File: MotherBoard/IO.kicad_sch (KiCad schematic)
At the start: 1 part, among them J1 1376357-3

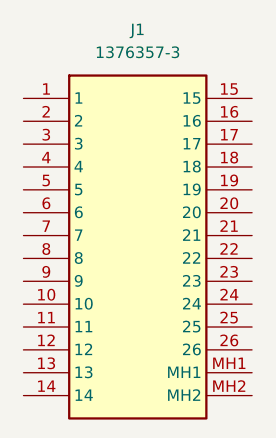
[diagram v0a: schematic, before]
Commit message: Complete bootstrap schematic for MCU
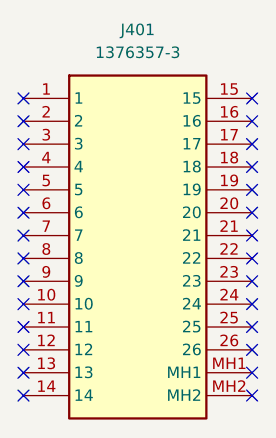
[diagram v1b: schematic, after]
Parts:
- renumbered J1 to J401
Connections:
- no-connect marks 0 -> 28
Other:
- title: IO Connector -> STM32 Layout
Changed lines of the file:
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@@
 	(paper "A4")
 	(title_block
-		(title "IO Connector")
+		(title "STM32 Layout")
 		(date "2024-10-15")
 		(rev "A")
 		(company "FSAE LSU")
+		(comment 1 "Jacob Parent ")
+		(comment 2 "parent.jacob7@protonmail.com")
+	)
+	(no_connect
+		(at 95.25 82.55)
+	)
+	(no_connect
+		(at 95.25 87.63)
+	)
+	(no_connect
+		(at 120.65 100.33)
+	)
+	(no_connect
+		(at 120.65 85.09)
+	)
+	(no_connect
+		(at 95.25 74.93)
+	)
+	(no_connect
+		(at 95.25 95.25)
+	)
+	(no_connect
+		(at 120.65 92.71)
+	)
+	(no_connect
+		(at 95.25 72.39)
+	)
+	(no_connect
+		(at 95.25 102.87)
+	)
+	(no_connect
+		(at 120.65 90.17)
+	)
+	(no_connect
+		(at 95.25 100.33)
+	)
+	(no_connect
+		(at 95.25 85.09)
+	)
+	(no_connect
+		(at 120.65 82.55)
+	)
+	(no_connect
+		(at 95.25 77.47)
+	)
+	(no_connect
+		(at 120.65 105.41)
+	)
+	(no_connect
+		(at 95.25 92.71)
+	)
+	(no_connect
+		(at 120.65 97.79)
+	)
+	(no_connect
+		(at 95.25 80.01)
+	)
+	(no_connect
+		(at 120.65 80.01)
+	)
+	(no_connect
+		(at 95.25 105.41)
+	)
+	(no_connect
+		(at 120.65 74.93)
+	)
+	(no_connect
+		(at 95.25 97.79)
+	)
+	(no_connect
+		(at 120.65 72.39)
+	)
+	(no_connect
+		(at 120.65 77.47)
+	)
+	(no_connect
+		(at 95.25 90.17)
+	)
+	(no_connect
+		(at 120.65 102.87)
+	)
+	(no_connect
+		(at 120.65 87.63)
+	)
+	(no_connect
+		(at 120.65 95.25)
 	)
 	(symbol
@@
 		(dnp no)
 		(fields_autoplaced yes)
-		(property "Reference" "J1"
+		(property "Reference" "J401"
 			(at 107.95 64.77 0)
 			(effects
@@
 		(pin "23"
 		)
-		(instances
-			(project ""
-				(path "/335e81e9-b957-4266-8116-dde74329bfca/a79abe16-9d7e-418f-82e9-de5f72e3bb16"
-					(reference "J1")
-					(unit 1)
-				)
-			)
-		)
+		(instances)
 	)
 )

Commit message: PSU Complete
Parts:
- renumbered J401 to J301
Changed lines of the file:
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@@
 		(dnp no)
 		(fields_autoplaced yes)
-		(property "Reference" "J401"
+		(property "Reference" "J301"
 			(at 107.95 64.77 0)
 			(effects
@@
 		(pin "23"
 		)
-		(instances)
+		(instances
+			(project ""
+				(path "/335e81e9-b957-4266-8116-dde74329bfca/a79abe16-9d7e-418f-82e9-de5f72e3bb16"
+					(reference "J301")
+					(unit 1)
+				)
+			)
+		)
 	)
 )

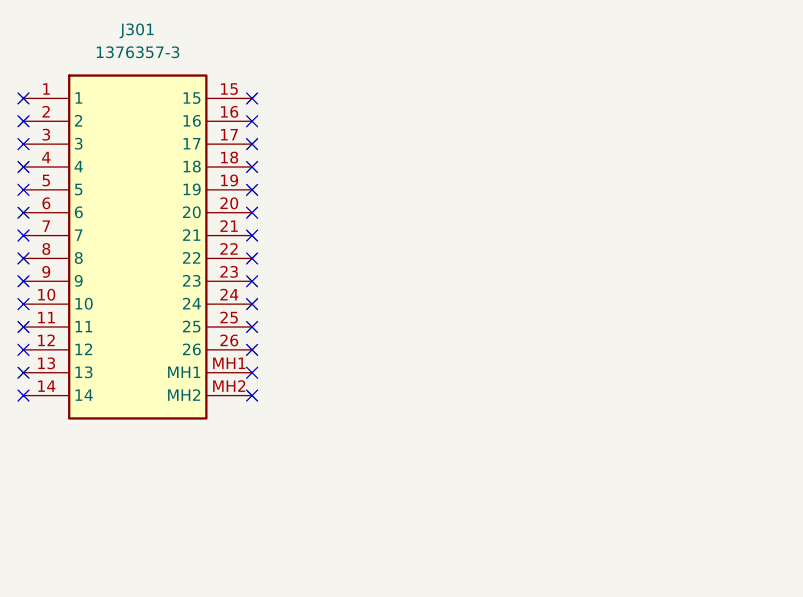
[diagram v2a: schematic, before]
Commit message: Added BQ7900 rough draft and TCAN
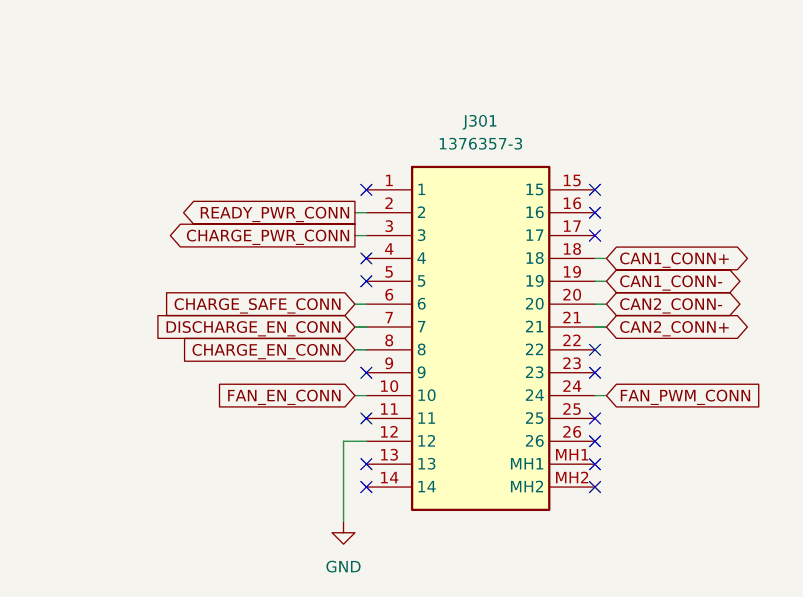
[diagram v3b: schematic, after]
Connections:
- net FAN_EN_CONN: now reaches J301.10
- net GND: now reaches J301.12
- net CAN1_CONN+: now reaches J301.18
- net CAN1_CONN-: now reaches J301.19
- net READY_PWR_CONN: now reaches J301.2
- net CAN2_CONN-: now reaches J301.20
- net CAN2_CONN+: now reaches J301.21
- net FAN_PWM_CONN: now reaches J301.24
- net CHARGE_PWR_CONN: now reaches J301.3
- net CHARGE_SAFE_CONN: now reaches J301.6
- net DISCHARGE_EN_CONN: now reaches J301.7
- net CHARGE_EN_CONN: now reaches J301.8
- no-connect marks 28 -> 16
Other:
- moved on the sheet: J301

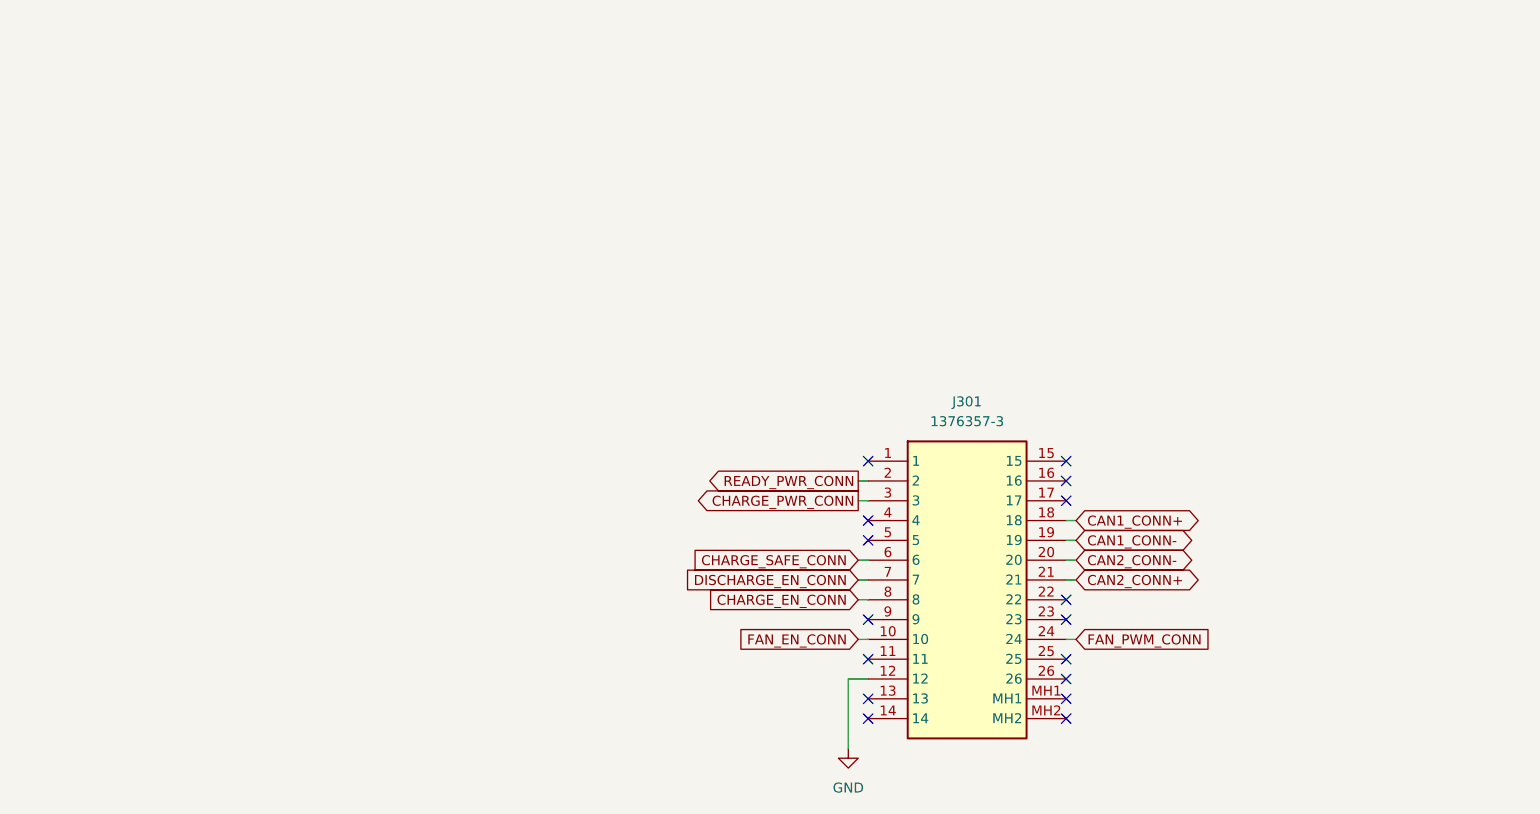
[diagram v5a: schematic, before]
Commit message: Fixed 3D model paths. Finished PSU ORing shcematic.
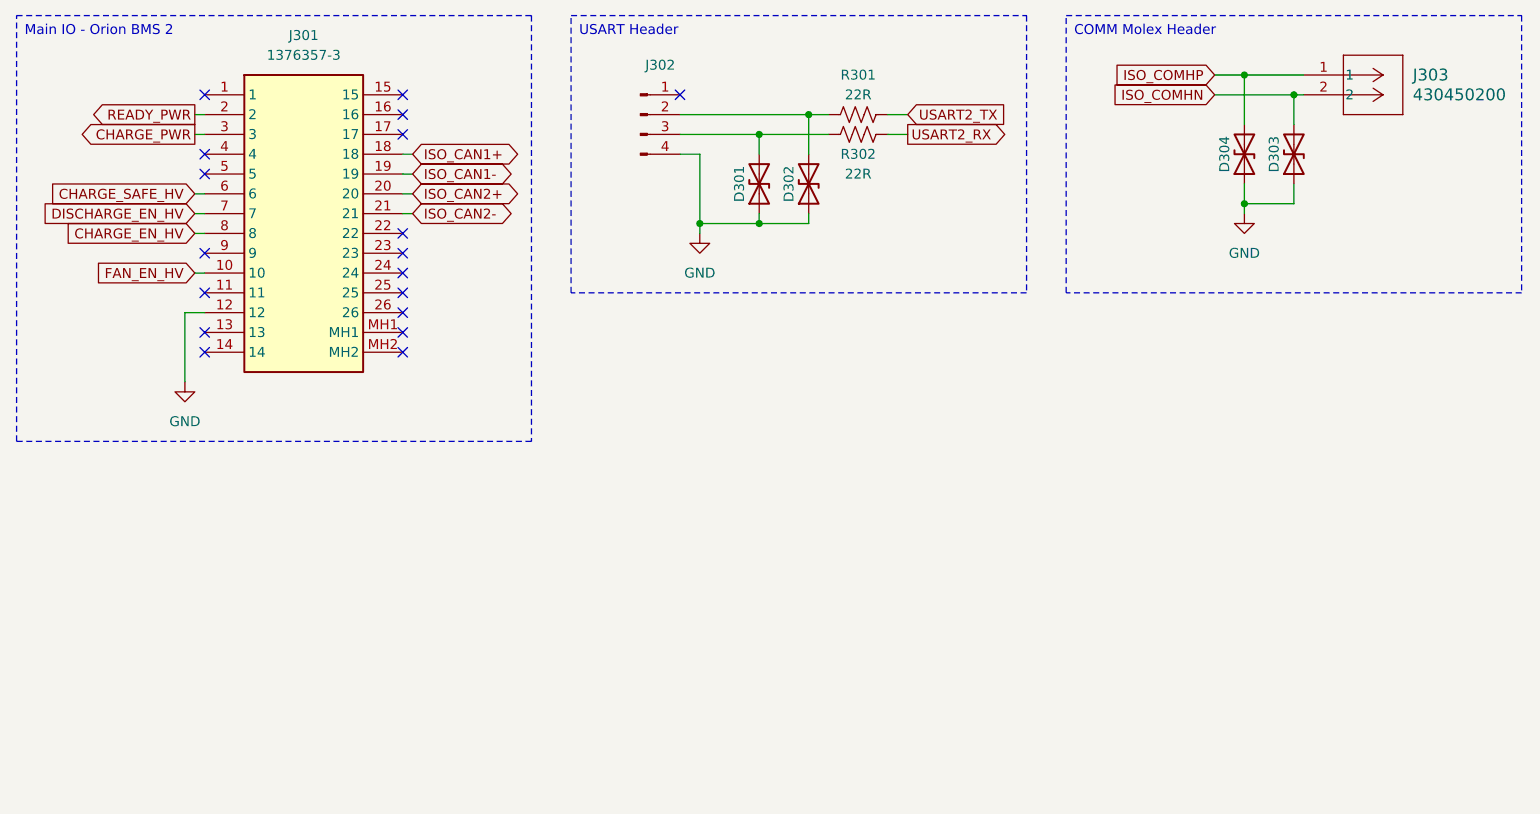
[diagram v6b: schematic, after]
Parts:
- added D301, D302, D303, D304: D_TVS, Diode_SMD:D_SOD-323, symbol Device:D_TVS
- added J302: Conn_01x04_Pin, symbol Connector:Conn_01x04_Pin
- added J303: 430450200, molex_comm:CON_430450200_MOL, symbol molex_comm:430450200
- added R301, R302: 22R, symbol Device:R_US
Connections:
- net GND: now also D301.1 (A1), D302.1 (A1), D303.1 (A1), D304.1 (A1), J302.4 (Pin_4)
- net CAN1_CONN+ renamed ISO_CAN1+
- net CAN1_CONN- renamed ISO_CAN1-
- net CAN2_CONN+ renamed ISO_CAN2-
- net CAN2_CONN- renamed ISO_CAN2+
- net CHARGE_EN_CONN renamed CHARGE_EN_HV
- net CHARGE_PWR_CONN renamed CHARGE_PWR
- net CHARGE_SAFE_CONN renamed CHARGE_SAFE_HV
- net DISCHARGE_EN_CONN renamed DISCHARGE_EN_HV
- net FAN_EN_CONN renamed FAN_EN_HV
- net FAN_PWM_CONN: no longer names the net of J301.24
- net READY_PWR_CONN renamed READY_PWR
- new net: D302.2 (A2), J302.2 (Pin_2), R301.1
- new net: D301.2 (A2), J302.3 (Pin_3), R302.1
- new net ISO_COMHN: D303.2 (A2), J303.2
- new net ISO_COMHP: D304.2 (A2), J303.1
- new net USART2_RX: R302.2
- new net USART2_TX: R301.2
- no-connect marks 16 -> 18
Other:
- moved on the sheet: J301

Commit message: Fixed relative paths + 90% footprints done + organized PCB for layout + found JLC part #s for manufacturing
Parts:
- D301, D302: Manufacturer_Part_Number (none) -> PESD3V3L1BA,115
- J302: footprint (none) -> Connector_PinHeader_2.54mm:PinHeader_1x04_P2.54mm_Vertical
- R301, R302: footprint (none) -> Resistor_SMD:R_0402_1005Metric

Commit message: Completed BOM except inductors
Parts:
- J301, J302, J303: now not fitted
- R301, R302: footprint Resistor_SMD:R_0402_1005Metric -> Resistor_SMD:R_1206_3216Metric; Manufacturer_Part_Number (none) -> FRC1206J220 TS
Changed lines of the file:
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@@
 		(in_bom yes)
 		(on_board yes)
-		(dnp no)
+		(dnp yes)
 		(property "Reference" "J302"
 			(at 106.68 31.75 0)
@@
 			)
 		)
-		(property "Footprint" "Resistor_SMD:R_0402_1005Metric"
+		(property "Footprint" "Resistor_SMD:R_1206_3216Metric"
 			(at 132.334 39.624 90)
 			(effects
@@
 		)
 		(property "Sim.Type" ""
+			(at 132.08 40.64 0)
+			(effects
+				(font
+					(size 1.27 1.27)
+				)
+				(hide yes)
+			)
+		)
+		(property "Manufacturer_Part_Number" "FRC1206J220 TS"
 			(at 132.08 40.64 0)
 			(effects
@@
 		(in_bom yes)
 		(on_board yes)
-		(dnp no)
+		(dnp yes)
 		(fields_autoplaced yes)
 		(property "Reference" "J301"
@@
 		(in_bom yes)
 		(on_board yes)
-		(dnp no)
+		(dnp yes)
 		(fields_autoplaced yes)
 		(property "Reference" "J303"
@@
 			)
 		)
-		(property "Footprint" "Resistor_SMD:R_0402_1005Metric"
+		(property "Footprint" "Resistor_SMD:R_1206_3216Metric"
 			(at 132.334 37.084 90)
 			(effects
@@
 			(at 132.08 38.1 0)
 			(effects
+				(font
+					(size 1.27 1.27)
+				)
+				(hide yes)
+			)
+		)
+		(property "Manufacturer_Part_Number" "FRC1206J220 TS"
+			(at 132.08 38.1 0)
+			(effects
